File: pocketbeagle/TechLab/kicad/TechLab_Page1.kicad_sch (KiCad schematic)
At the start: 40 parts, among them J4 Conn_01x02, P1 Conn_02x18_Odd_Even, P2 Conn_02x18_Odd_Even, U1 CAT24C32, U2 TPD4S012DRY, U3 MMA8453Q, U4 TPS2051CDBV, X1 292303-1

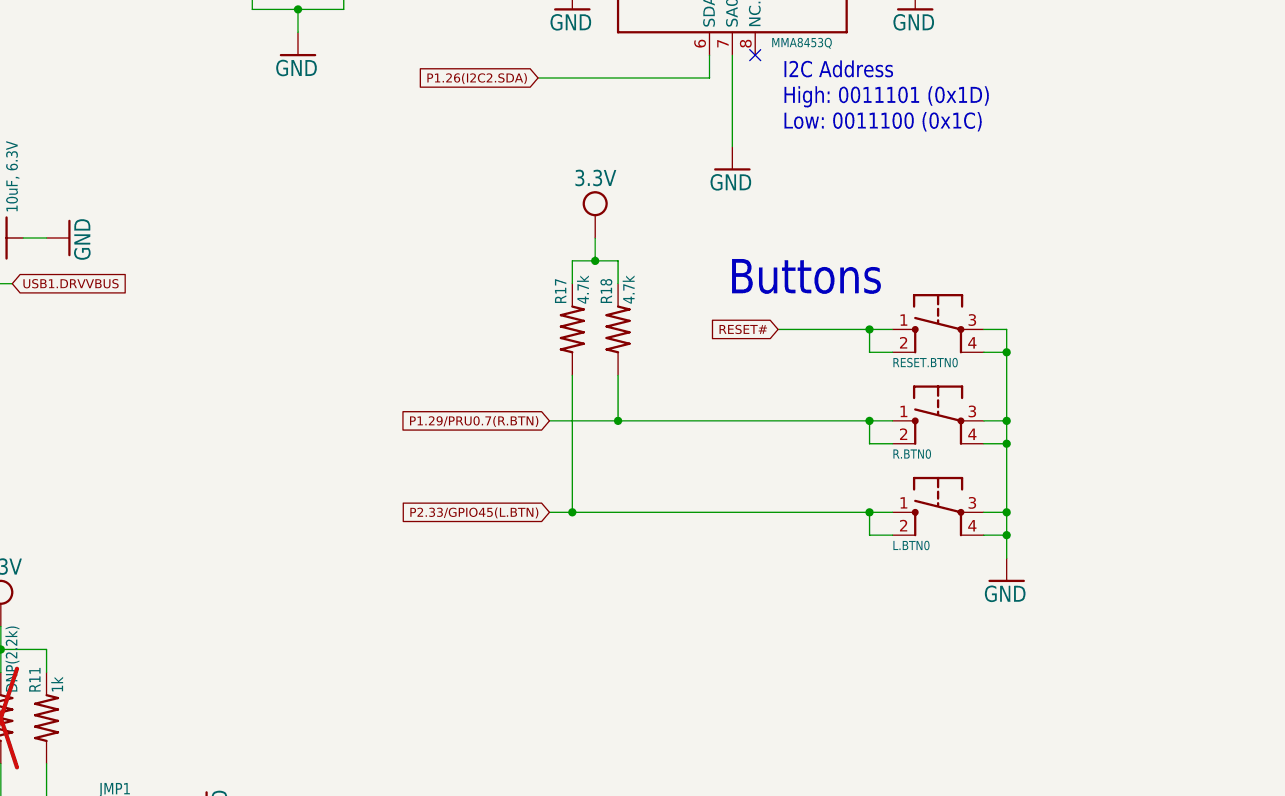
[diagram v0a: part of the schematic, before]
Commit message: Add I2C port
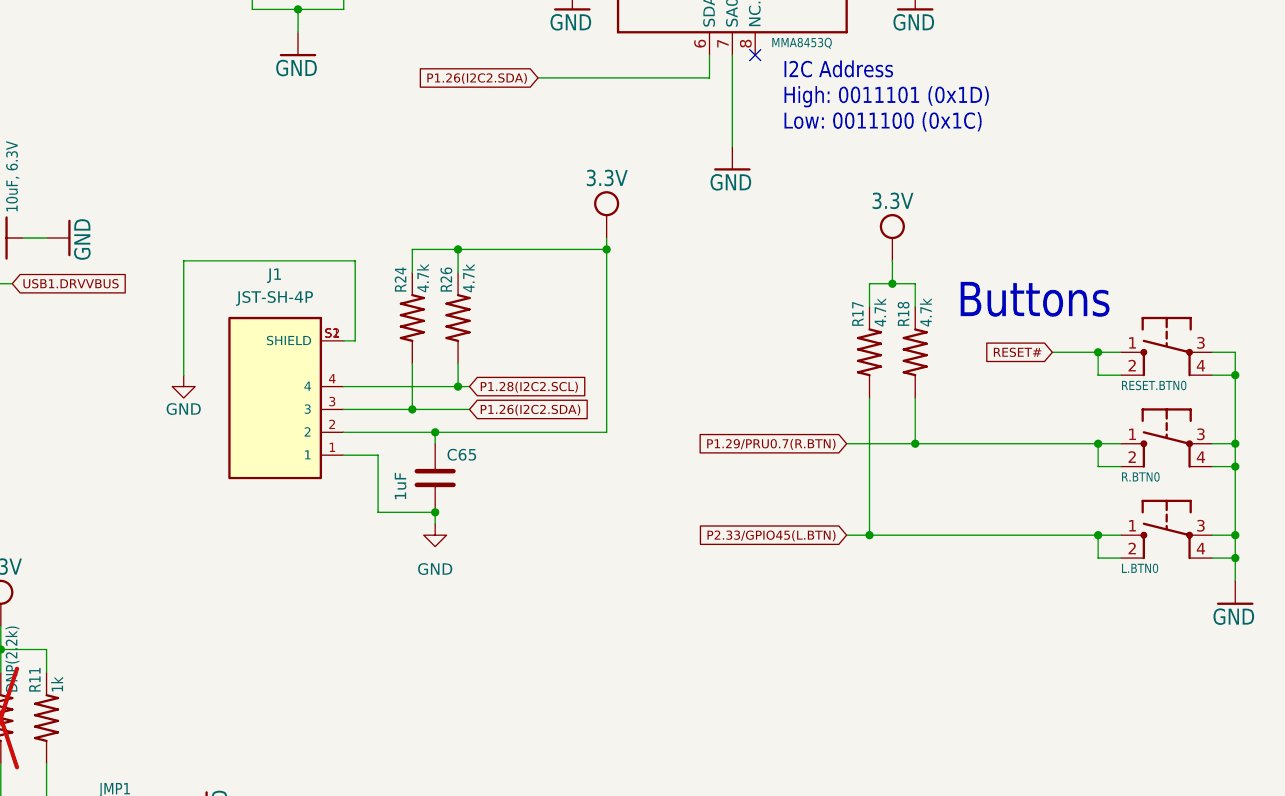
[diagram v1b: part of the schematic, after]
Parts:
- added C65: 1uF, Capacitor_SMD:C_0603_1608Metric_Pad1.08x0.95mm_HandSolder, symbol Device:C
- added J1: JST-SH-4P, Upside Down Labs:JST-SH-4P, symbol Upside Down Labs:JST-SH-4P
- added R24, R26: 4.7k, TechLab:0402, symbol TechLab-eagle-import:RESISTOR-(INCH)-0402
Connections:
- net 3.3V: now also C65.1, J1.2, R24.2, R26.2
- net GND: now also C65.2, J1.1, J1.S1 (SHIELD), J1.S2 (SHIELD)
- net P1.26(I2C2.SDA): now also J1.3, R24.1
- net P1.28(I2C2.SCL): now also J1.4, R26.1
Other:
- moved on the sheet: L.BTN0, R.BTN0, R17, R18, RESET.BTN0
